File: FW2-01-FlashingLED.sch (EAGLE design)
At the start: 12 parts, among them Q1 BC547, Q3 BC547

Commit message: Basic board layout. Maybe almost done, needs a review
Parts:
- removed JP3: PWR+, freetronics-master-v1.1:M01PTH
- removed JP4: PWR-, freetronics-master-v1.1:M01PTH
- removed Q3: BC547, freetronics-master-v1.1:BC547
- added JP1: PWR+, freetronics-master-v1.1:M01PTH
- added JP2: PWR-, freetronics-master-v1.1:M01PTH
- added Q2: BC547, freetronics-master-v1.1:BC547
- C1: value 2.2uF -> 10uF; device SparkFun:CAP_POLPTH1 -> adafruit:CPOL-USE5-5
- C2: device SparkFun:CAP_POLPTH1 -> adafruit:CPOL-USE5-5
- R1, R4: value 4K7 -> 330R
- R2, R3: value 4K7 -> 47K
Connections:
- new net N$2: JP1.1, LED1.A, LED2.A, R2.2, R3.2
- new net N$3: C1.+, Q1.C, R1.1
- new net N$4: C2.+, Q2.C, R4.1
- new net N$5: LED2.C, R4.2
- new net N$7: C2.-, Q1.B, R3.1
- new net N$8: C1.-, Q2.B, R2.1
- new net N$9: JP2.1, Q1.E, Q2.E
- net N$1: now also R1.2; no longer R2.2
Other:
- note added: "3-12Vdc"
- note added: "Flashing LED (Funway compatible)"
- note added: "V1.0 (2016-10-08)"
- note added: "www.freetronics.com.au/fw2-flash"
- note removed: "9V"
- note removed: "INPUT"
- note removed: "LED Level Display (Funway compatible)"
- note removed: "V1.0 (2016-10-06)"
- note removed: "www.freetronics.com.au/fw2-level"
- moved on the sheet: C1, C2, LED2, Q1, R1, R2, R3, R4

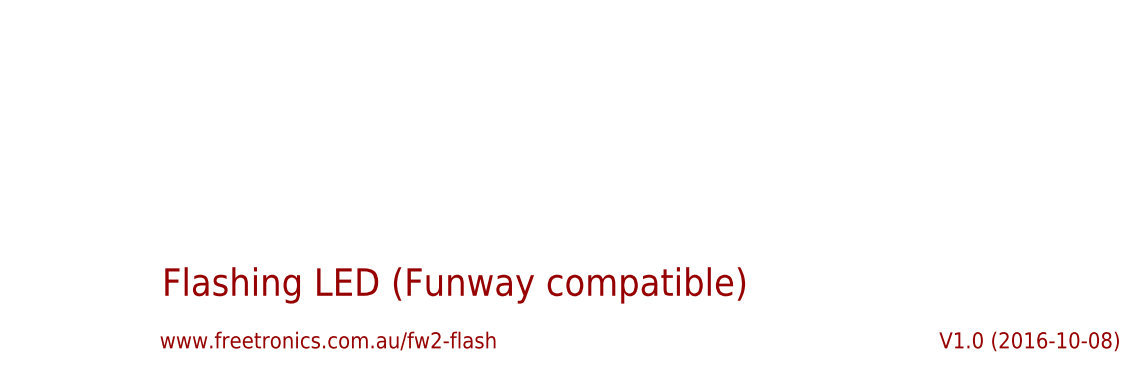
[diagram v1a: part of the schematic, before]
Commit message: Updated silkscreen and labels
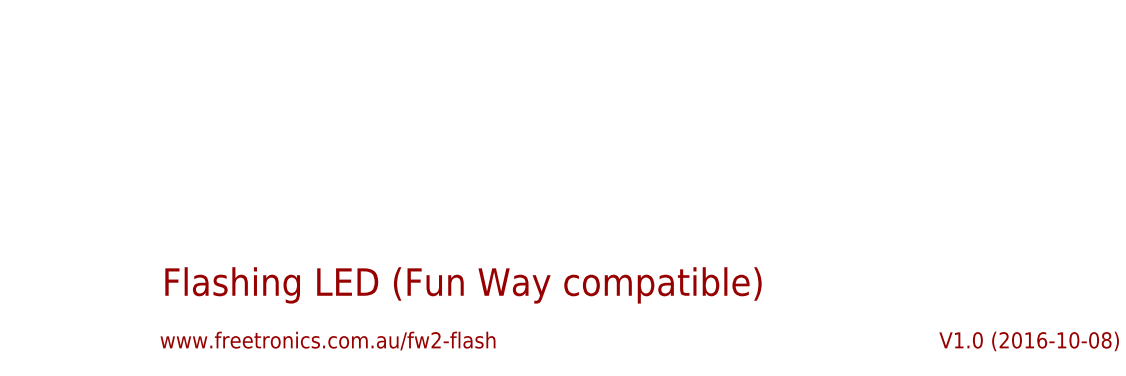
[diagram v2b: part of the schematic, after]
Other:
- note added: "Flashing LED (Fun Way compatible)"
- note removed: "Flashing LED (Funway compatible)"
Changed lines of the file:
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@@
 <sheet>
 <plain>
-<text x="129.54" y="12.7" size="3.048" layer="94">Flashing LED (Funway compatible)</text>
+<text x="129.54" y="12.7" size="3.048" layer="94">Flashing LED (Fun Way compatible)</text>
 <text x="215.9" y="6.858" size="1.778" layer="94">V1.0 (2016-10-08)</text>
 <text x="129.286" y="6.858" size="1.778" layer="94">www.freetronics.com.au/fw2-flash</text>

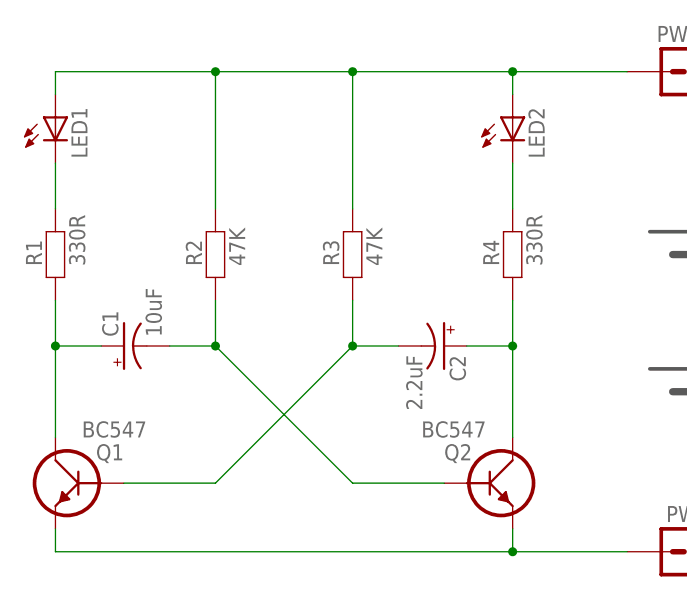
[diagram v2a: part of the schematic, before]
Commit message: Increased pad size and track width
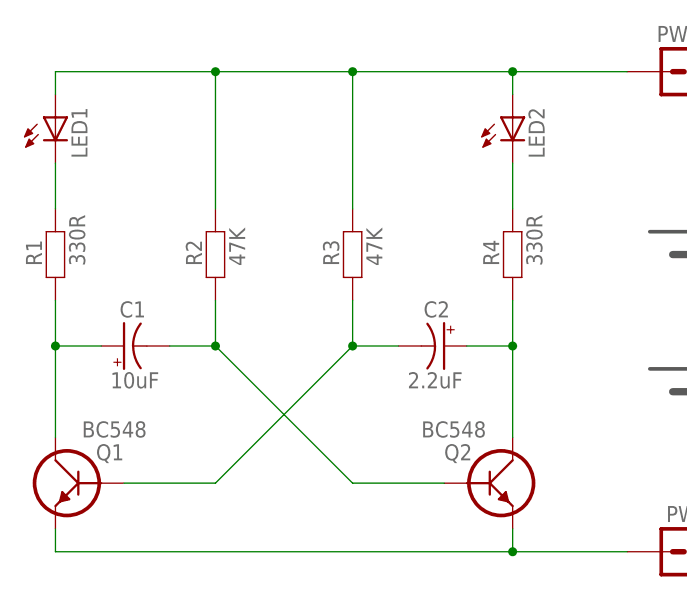
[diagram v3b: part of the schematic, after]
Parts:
- LED1, LED2: device freetronics-master-v1.1:LED5MM -> freetronics-master-v1.1:LED5MML
- Q1, Q2: value BC547 -> BC548
- R1, R2, R3, R4: device freetronics:FREETRONICS_RESISTORPTH2 -> freetronics:FREETRONICS_RESISTORPTH3
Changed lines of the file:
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@@
 <setting verticaltext="up"/>
 </settings>
-<grid distance="0.1" unitdist="inch" unit="inch" style="lines" multiple="1" display="no" altdistance="0.01" altunitdist="inch" altunit="inch"/>
+<grid distance="0.05" unitdist="inch" unit="inch" style="lines" multiple="1" display="no" altdistance="0.01" altunitdist="inch" altunit="inch"/>
 <layers>
 <layer number="1" name="Top" color="4" fill="1" visible="no" active="no"/>
@@
 </classes>
 <parts>
-<part name="LED1" library="freetronics-master-v1.1" deviceset="LED" device="5MM"/>
-<part name="Q2" library="freetronics-master-v1.1" deviceset="BC547" device=""/>
+<part name="LED1" library="freetronics-master-v1.1" deviceset="LED" device="5MML"/>
+<part name="Q2" library="freetronics-master-v1.1" deviceset="BC547" device="" value="BC548"/>
 <part name="JP1" library="freetronics-master-v1.1" deviceset="M01" device="PTH" value="PWR+"/>
 <part name="JP2" library="freetronics-master-v1.1" deviceset="M01" device="PTH" value="PWR-"/>
 <part name="C2" library="adafruit" deviceset="CPOL-US" device="E5-5" value="2.2uF"/>
-<part name="R1" library="freetronics" deviceset="FREETRONICS_RESISTOR" device="PTH2" value="330R"/>
-<part name="Q1" library="freetronics-master-v1.1" deviceset="BC547" device=""/>
-<part name="R2" library="freetronics" deviceset="FREETRONICS_RESISTOR" device="PTH2" value="47K"/>
-<part name="R3" library="freetronics" deviceset="FREETRONICS_RESISTOR" device="PTH2" value="47K"/>
-<part name="R4" library="freetronics" deviceset="FREETRONICS_RESISTOR" device="PTH2" value="330R"/>
+<part name="R1" library="freetronics" deviceset="FREETRONICS_RESISTOR" device="PTH3" value="330R"/>
+<part name="Q1" library="freetronics-master-v1.1" deviceset="BC547" device="" value="BC548"/>
+<part name="R2" library="freetronics" deviceset="FREETRONICS_RESISTOR" device="PTH3" value="47K"/>
+<part name="R3" library="freetronics" deviceset="FREETRONICS_RESISTOR" device="PTH3" value="47K"/>
+<part name="R4" library="freetronics" deviceset="FREETRONICS_RESISTOR" device="PTH3" value="330R"/>
 <part name="C1" library="adafruit" deviceset="CPOL-US" device="E5-5" value="10uF"/>
-<part name="LED2" library="freetronics-master-v1.1" deviceset="LED" device="5MM"/>
+<part name="LED2" library="freetronics-master-v1.1" deviceset="LED" device="5MML"/>
 </parts>
 <sheets>
@@
 </plain>
 <instances>
-<instance part="LED1" gate="G$1" x="78.74" y="121.92"/>
+<instance part="LED1" gate="G$1" x="78.74" y="121.92" smashed="yes">
+<attribute name="NAME" x="82.296" y="117.348" size="1.778" layer="95" rot="R90"/>
+<attribute name="VALUE" x="84.455" y="117.348" size="1.778" layer="96" rot="R90"/>
+</instance>
 <instance part="Q2" gate="G$1" x="127" y="81.28" smashed="yes">
 <attribute name="NAME" x="121.92" y="83.82" size="1.778" layer="95"/>
@@
 <instance part="JP1" gate="G$1" x="149.86" y="127" rot="R180"/>
 <instance part="JP2" gate="G$1" x="149.86" y="73.66" rot="R180"/>
-<instance part="C2" gate="G$1" x="121.92" y="96.52" rot="R270"/>
+<instance part="C2" gate="G$1" x="121.92" y="96.52" smashed="yes" rot="R270">
+<attribute name="NAME" x="119.634" y="99.695" size="1.778" layer="95"/>
+<attribute name="VALUE" x="117.856" y="91.821" size="1.778" layer="96"/>
+</instance>
 <instance part="R1" gate="G$1" x="78.74" y="106.68" smashed="yes" rot="R90">
 <attribute name="NAME" x="77.2414" y="105.41" size="1.778" layer="95" rot="R90"/>
@@
 <attribute name="VALUE" x="132.842" y="105.41" size="1.778" layer="96" rot="R90"/>
 </instance>
-<instance part="C1" gate="G$1" x="86.36" y="96.52" rot="R90"/>
-<instance part="LED2" gate="G$1" x="129.54" y="121.92"/>
+<instance part="C1" gate="G$1" x="86.36" y="96.52" smashed="yes" rot="R90">
+<attribute name="NAME" x="85.852" y="99.695" size="1.778" layer="95"/>
+<attribute name="VALUE" x="84.836" y="91.821" size="1.778" layer="96"/>
+</instance>
+<instance part="LED2" gate="G$1" x="129.54" y="121.92" smashed="yes">
+<attribute name="NAME" x="133.096" y="117.348" size="1.778" layer="95" rot="R90"/>
+<attribute name="VALUE" x="135.255" y="117.348" size="1.778" layer="96" rot="R90"/>
+</instance>
 </instances>
 <busses>
@@
 </sheet>
 </sheets>
+<errors>
+</errors>
 </schematic>
 </drawing>
